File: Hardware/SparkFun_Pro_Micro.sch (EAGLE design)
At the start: 38 parts, among them J2 Qwiic, U1 3.3V, U3 ATmega32U4, Y2 32MHz

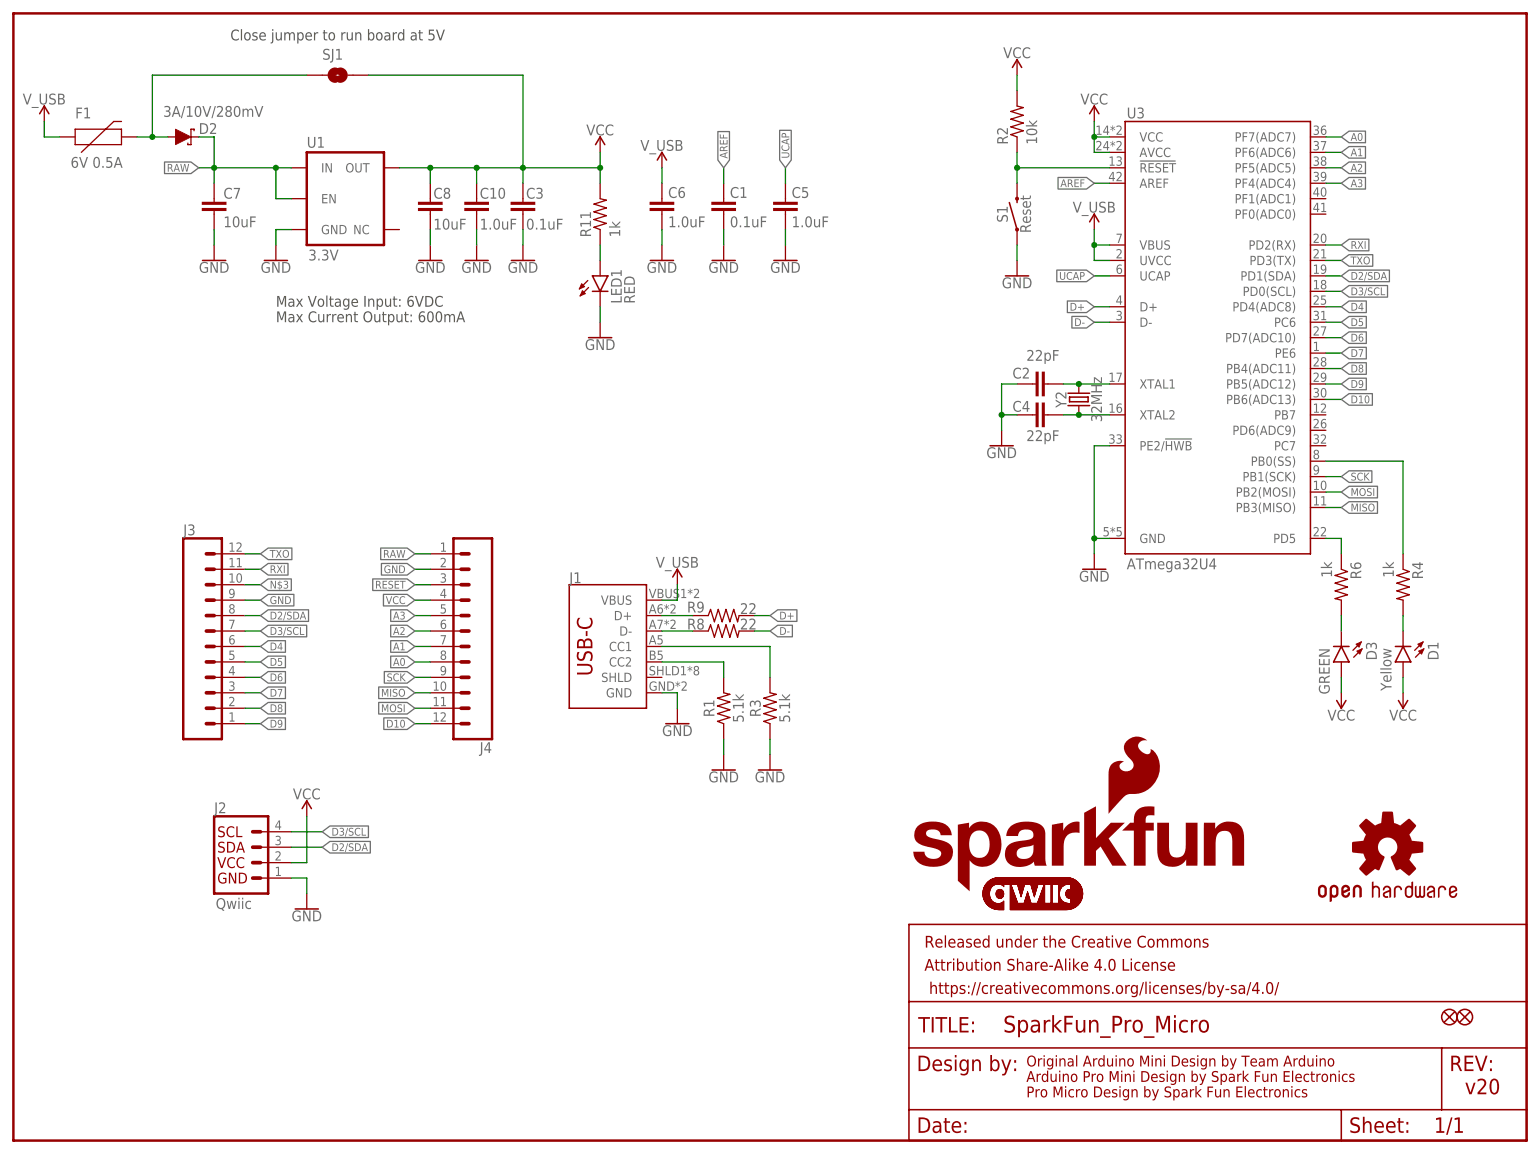
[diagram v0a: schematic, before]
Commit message: Rev to USB C
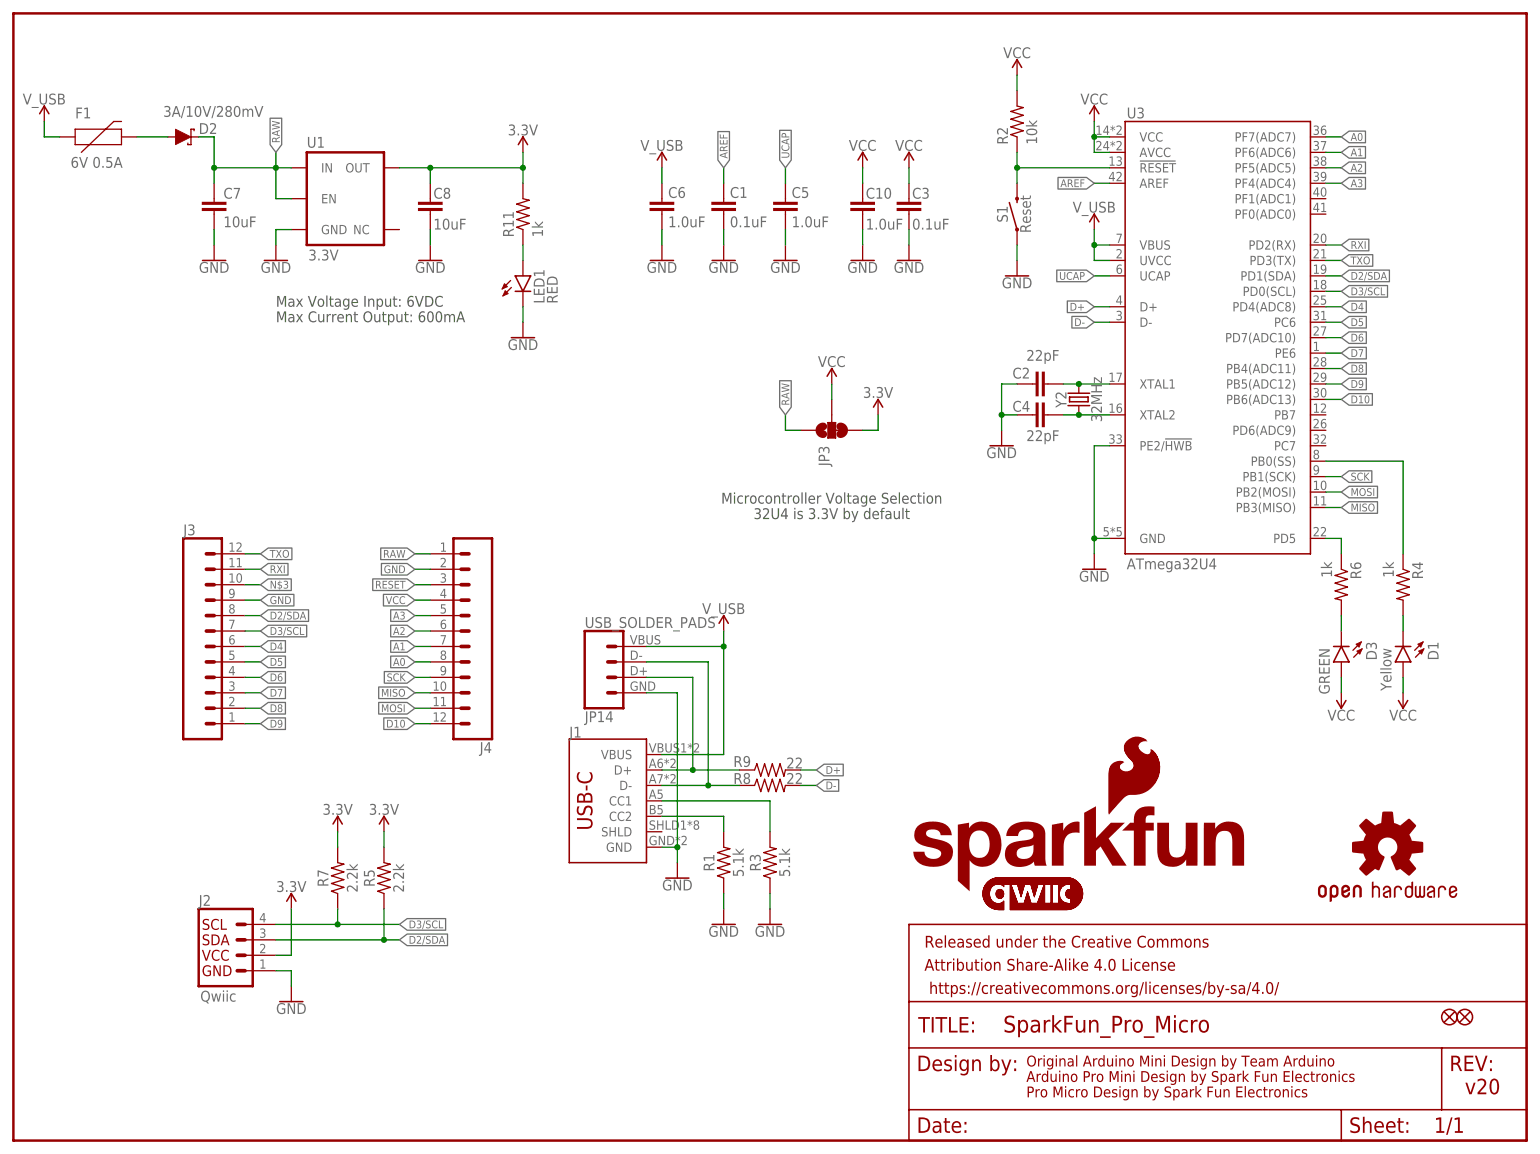
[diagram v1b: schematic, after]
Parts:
- removed SJ1: Closed for 5V Board, SparkFun-Jumpers:JUMPER-SMT_2_NO_SILK
- added JP14: USB_SOLDER_PADS, SparkFun-Connectors:USB_SOLDER_PADS
- added JP3: JUMPER-SMT_3_1-NC_TRACE_SILK, SparkFun-Jumpers:JUMPER-SMT_3_1-NC_TRACE_SILK
- added LOGO4: SFE_LOGO_FLAME.1_INCH, SparkFun-Aesthetics:SFE_LOGO_FLAME.1_INCH
- added R5, R7: 2.2k, SparkFun-Resistors:2.2KOHM-0402T-1/16W-1%
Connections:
- new net 3.3V: C8.2, J2.2, JP3.3, R11.2, R5.2, R7.2, U1.OUT
- net D-_HV: now also JP14.2
- net D2/SDA: now also R5.1
- net D3/SCL: now also R7.1
- net DP_HV: now also JP14.3
- net GND: now also JP14.4
- net RAW: now also JP3.1
- net USB_RAW: no longer SJ1.1
- net VCC: now also JP3.2; no longer C8.2, J2.2, R11.2, SJ1.2, U1.OUT
- net V_USB: now also JP14.1
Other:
- note added: "32U4 is 3.3V by default"
- note added: "Microcontroller Voltage Selection"
- note removed: "Close jumper to run board at 5V"
- moved on the sheet: C10, C3, J1, J2, LED1, R1, R11, R3, R8, R9

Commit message: Commit before ordering v20
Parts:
- removed J1: (no value), USBC:USB_C4
- added J5: (no value), USBC:USB_C5
- renumbered JP3 to JP4
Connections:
- net 3.3V: now also JP4.1; no longer JP4.3
- net D-_HV: now also J5.D-; no longer J1.D-
- net DP_HV: now also J5.D+; no longer J1.D+
- net GND: now also J5.GND; no longer J1.GND
- net N$10: now also J5.CC2; no longer J1.CC2
- net N$9: now also J5.CC1; no longer J1.CC1
- net RAW: now also JP4.3; no longer JP4.1
- net V_USB: now also J5.VBUS; no longer J1.VBUS
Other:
- note added: "32U4 is 5V by default I2C Bus is still 3.3V"
- note removed: "32U4 is 3.3V by default"

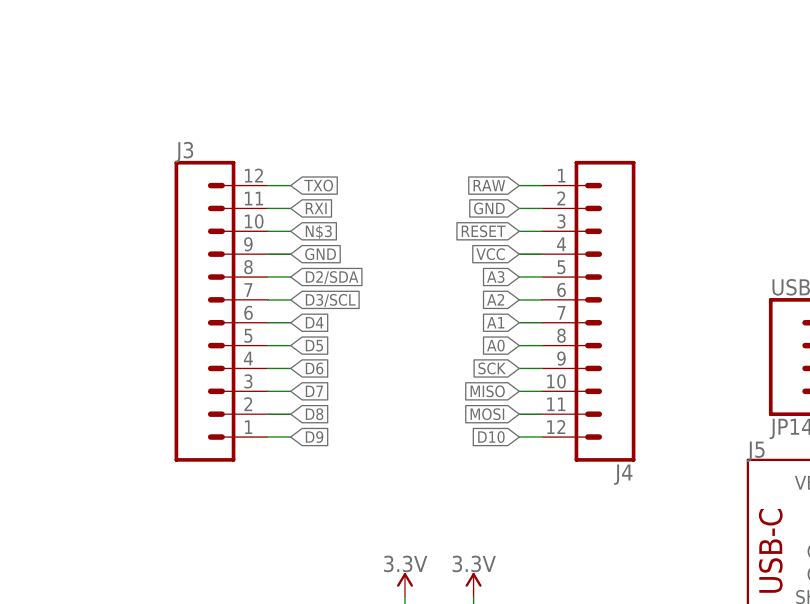
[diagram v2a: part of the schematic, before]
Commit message: Updates to Pro Micro and Frank
"Castellated" library '1x12CASTELLATED' and 'PRO_MICRO_C' footprints updated and 'PRO_MICRO_C' device updated.

Pro Micro C got uniform drill/ring sizing + added plated holes to outside in place of drills

Frank got 1U Keycap standard switch spacing and updated Pro Micro footprint.
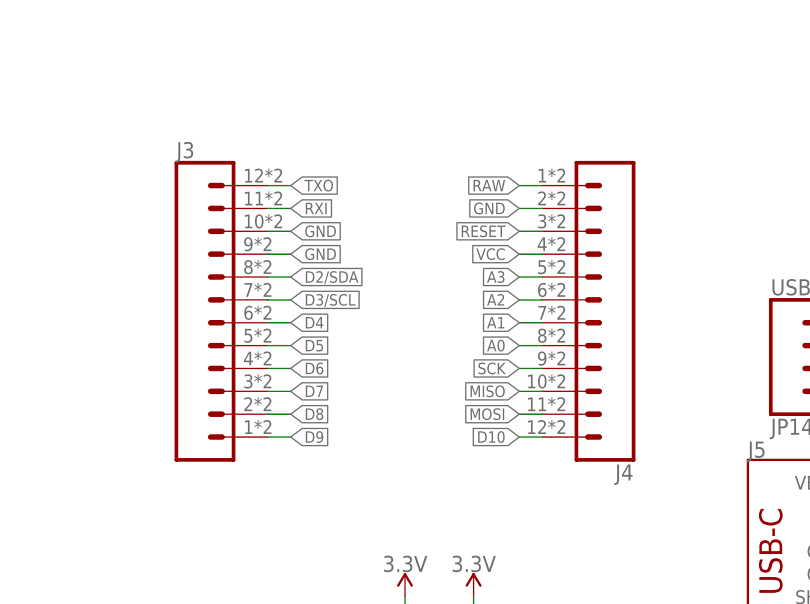
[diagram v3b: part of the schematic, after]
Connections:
- removed net N$3: J3.10
- net GND: now also J3.10
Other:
- moved on the sheet: J3, J4
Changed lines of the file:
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@@
 <grid distance="0.1" unitdist="inch" unit="inch" style="lines" multiple="1" display="no" altdistance="0.01" altunitdist="inch" altunit="inch"/>
 <layers>
-<layer number="1" name="Top" color="4" fill="1" visible="yes" active="no"/>
-<layer number="2" name="Route2" color="1" fill="3" visible="yes" active="no"/>
-<layer number="3" name="Route3" color="4" fill="3" visible="yes" active="no"/>
-<layer number="4" name="Route4" color="1" fill="4" visible="yes" active="no"/>
-<layer number="5" name="Route5" color="4" fill="4" visible="yes" active="no"/>
-<layer number="6" name="Route6" color="1" fill="8" visible="yes" active="no"/>
-<layer number="7" name="Route7" color="4" fill="8" visible="yes" active="no"/>
-<layer number="8" name="Route8" color="1" fill="2" visible="yes" active="no"/>
-<layer number="9" name="Route9" color="4" fill="2" visible="yes" active="no"/>
-<layer number="10" name="Route10" color="1" fill="7" visible="yes" active="no"/>
-<layer number="11" name="Route11" color="4" fill="7" visible="yes" active="no"/>
-<layer number="12" name="Route12" color="1" fill="5" visible="yes" active="no"/>
-<layer number="13" name="Route13" color="4" fill="5" visible="yes" active="no"/>
-<layer number="14" name="Route14" color="1" fill="6" visible="yes" active="no"/>
-<layer number="15" name="Route15" color="4" fill="6" visible="yes" active="no"/>
-<layer number="16" name="Bottom" color="1" fill="1" visible="yes" active="no"/>
-<layer number="17" name="Pads" color="2" fill="1" visible="yes" active="no"/>
-<layer number="18" name="Vias" color="2" fill="1" visible="yes" active="no"/>
-<layer number="19" name="Unrouted" color="6" fill="1" visible="yes" active="no"/>
-<layer number="20" name="Dimension" color="24" fill="1" visible="yes" active="no"/>
-<layer number="21" name="tPlace" color="16" fill="1" visible="yes" active="no"/>
-<layer number="22" name="bPlace" color="14" fill="1" visible="yes" active="no"/>
-<layer number="23" name="tOrigins" color="15" fill="1" visible="yes" active="no"/>
-<layer number="24" name="bOrigins" color="15" fill="1" visible="yes" active="no"/>
-<layer number="25" name="tNames" color="7" fill="1" visible="yes" active="no"/>
-<layer number="26" name="bNames" color="7" fill="1" visible="yes" active="no"/>
-<layer number="27" name="tValues" color="7" fill="1" visible="yes" active="no"/>
-<layer number="28" name="bValues" color="7" fill="1" visible="yes" active="no"/>
+<layer number="1" name="Top" color="4" fill="1" visible="no" active="no"/>
+<layer number="2" name="Route2" color="1" fill="3" visible="no" active="no"/>
+<layer number="3" name="Route3" color="4" fill="3" visible="no" active="no"/>
+<layer number="4" name="Route4" color="1" fill="4" visible="no" active="no"/>
+<layer number="5" name="Route5" color="4" fill="4" visible="no" active="no"/>
+<layer number="6" name="Route6" color="1" fill="8" visible="no" active="no"/>
+<layer number="7" name="Route7" color="4" fill="8" visible="no" active="no"/>
+<layer number="8" name="Route8" color="1" fill="2" visible="no" active="no"/>
+<layer number="9" name="Route9" color="4" fill="2" visible="no" active="no"/>
+<layer number="10" name="Route10" color="1" fill="7" visible="no" active="no"/>
+<layer number="11" name="Route11" color="4" fill="7" visible="no" active="no"/>
+<layer number="12" name="Route12" color="1" fill="5" visible="no" active="no"/>
+<layer number="13" name="Route13" color="4" fill="5" visible="no" active="no"/>
+<layer number="14" name="Route14" color="1" fill="6" visible="no" active="no"/>
+<layer number="15" name="Route15" color="4" fill="6" visible="no" active="no"/>
+<layer number="16" name="Bottom" color="1" fill="1" visible="no" active="no"/>
+<layer number="17" name="Pads" color="2" fill="1" visible="no" active="no"/>
+<layer number="18" name="Vias" color="2" fill="1" visible="no" active="no"/>
+<layer number="19" name="Unrouted" color="6" fill="1" visible="no" active="no"/>
+<layer number="20" name="Dimension" color="24" fill="1" visible="no" active="no"/>
+<layer number="21" name="tPlace" color="16" fill="1" visible="no" active="no"/>
+<layer number="22" name="bPlace" color="14" fill="1" visible="no" active="no"/>
+<layer number="23" name="tOrigins" color="15" fill="1" visible="no" active="no"/>
+<layer number="24" name="bOrigins" color="15" fill="1" visible="no" active="no"/>
+<layer number="25" name="tNames" color="7" fill="1" visible="no" active="no"/>
+<layer number="26" name="bNames" color="7" fill="1" visible="no" active="no"/>
+<layer number="27" name="tValues" color="7" fill="1" visible="no" active="no"/>
+<layer number="28" name="bValues" color="7" fill="1" visible="no" active="no"/>
 <layer number="29" name="tStop" color="7" fill="3" visible="no" active="no"/>
 <layer number="30" name="bStop" color="7" fill="6" visible="no" active="no"/>
@@
 <layer number="35" name="tGlue" color="7" fill="4" visible="no" active="no"/>
 <layer number="36" name="bGlue" color="7" fill="5" visible="no" active="no"/>
-<layer number="37" name="tTest" color="7" fill="1" visible="yes" active="no"/>
-<layer number="38" name="bTest" color="7" fill="1" visible="yes" active="no"/>
+<layer number="37" name="tTest" color="7" fill="1" visible="no" active="no"/>
+<layer number="38" name="bTest" color="7" fill="1" visible="no" active="no"/>
 <layer number="39" name="tKeepout" color="4" fill="11" visible="no" active="no"/>
 <layer number="40" name="bKeepout" color="1" fill="11" visible="no" active="no"/>
@@
 <layer number="44" name="Drills" color="7" fill="1" visible="no" active="no"/>
 <layer number="45" name="Holes" color="7" fill="1" visible="no" active="no"/>
-<layer number="46" name="Milling" color="3" fill="1" visible="yes" active="no"/>
-<layer number="47" name="Measures" color="7" fill="1" visible="yes" active="no"/>
-<layer number="48" name="Document" color="7" fill="1" visible="yes" active="no"/>
-<layer number="49" name="Reference" color="7" fill="1" visible="yes" active="no"/>
-<layer number="50" name="dxf" color="7" fill="1" visible="yes" active="no"/>
-<layer number="51" name="tDocu" color="6" fill="1" visible="yes" active="no"/>
-<layer number="52" name="bDocu" color="7" fill="1" visible="yes" active="no"/>
-<layer number="53" name="tGND_GNDA" color="7" fill="9" visible="yes" active="no"/>
-<layer number="54" name="bGND_GNDA" color="1" fill="9" visible="yes" active="no"/>
-<layer number="56" name="wert" color="7" fill="1" visible="yes" active="no"/>
-<layer number="57" name="tCAD" color="7" fill="1" visible="yes" active="no"/>
-<layer number="59" name="tCarbon" color="7" fill="1" visible="yes" active="no"/>
-<layer number="60" name="bCarbon" color="7" fill="1" visible="yes" active="no"/>
+<layer number="46" name="Milling" color="3" fill="1" visible="no" active="no"/>
+<layer number="47" name="Measures" color="7" fill="1" visible="no" active="no"/>
+<layer number="48" name="Document" color="7" fill="1" visible="no" active="no"/>
+<layer number="49" name="Reference" color="7" fill="1" visible="no" active="no"/>
+<layer number="50" name="dxf" color="7" fill="1" visible="no" active="no"/>
+<layer number="51" name="tDocu" color="6" fill="1" visible="no" active="no"/>
+<layer number="52" name="bDocu" color="7" fill="1" visible="no" active="no"/>
+<layer number="53" name="tGND_GNDA" color="7" fill="9" visible="no" active="no"/>
+<layer number="54" name="bGND_GNDA" color="1" fill="9" visible="no" active="no"/>
+<layer number="56" name="wert" color="7" fill="1" visible="no" active="no"/>
+<layer number="57" name="tCAD" color="7" fill="1" visible="no" active="no"/>
+<layer number="59" name="tCarbon" color="7" fill="1" visible="no" active="no"/>
+<layer number="60" name="bCarbon" color="7" fill="1" visible="no" active="no"/>
 <layer number="88" name="SimResults" color="9" fill="1" visible="yes" active="yes"/>
 <layer number="89" name="SimProbes" color="9" fill="1" visible="yes" active="yes"/>
@@
 <pinref part="GND16" gate="1" pin="GND"/>
 </segment>
+<segment>
+<wire x1="38.1" y1="91.44" x2="40.64" y2="91.44" width="0.1524" layer="91"/>
+<label x="40.64" y="91.44" size="1.27" layer="95" xref="yes"/>
+<pinref part="J3" gate="G$1" pin="10"/>
+</segment>
 </net>
 <net name="AREF" class="0">
@@
 </segment>
 </net>
-<net name="N$3" class="0">
-<segment>
-<wire x1="38.1" y1="91.44" x2="40.64" y2="91.44" width="0.1524" layer="91"/>
-<label x="40.64" y="91.44" size="1.27" layer="95" xref="yes"/>
-<pinref part="J3" gate="G$1" pin="10"/>
-</segment>
-</net>

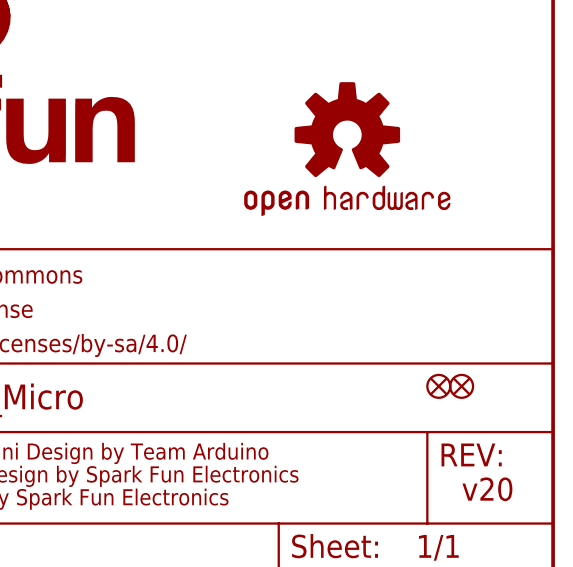
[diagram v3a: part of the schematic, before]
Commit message: Red boards ordered
Modify castellated 1x12 to larger diameter plated castellated holes. Panelize with route-out around castellated edges. Scoot Qwiic connector in to use that side of the board as the tab.
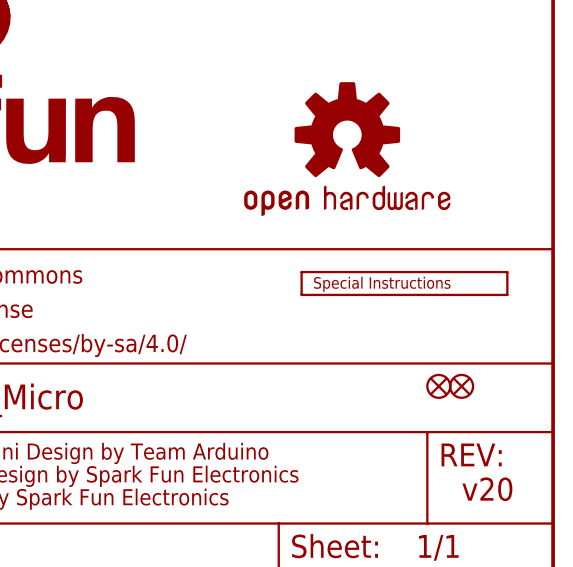
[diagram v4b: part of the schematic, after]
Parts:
- added LOGO5: SPECIAL_INSTRUCTIONS-ORDERING, SparkFun-Aesthetics:SPECIAL_INSTRUCTIONS-ORDERING
